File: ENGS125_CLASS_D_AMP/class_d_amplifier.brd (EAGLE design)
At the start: 89.8 x 64.8 mm, 24 parts, among them J1 BANANA_JACK_CT3151, J2 BANANA_JACK_CT3151, J3 BANANA_JACK_CT3151, J4 BANANA_JACK_CT3151, J5 BANANA_JACK_CT3151, J6 BANANA_JACK_CT3151, M1 BSC050NE2LSATMA1, M2 BSC050NE2LSATMA1, U1 LTC6992TSOT-23, U2 LTC4449

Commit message: Added Thayer shield to silkscreen on layout
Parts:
- added U$1: THAYER, Engs125_lib_UPDATEFeb22_with_logo:THAYER
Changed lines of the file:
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@@
 <layer number="25" name="tNames" color="7" fill="1" visible="yes" active="yes"/>
 <layer number="26" name="bNames" color="7" fill="1" visible="yes" active="yes"/>
-<layer number="27" name="tValues" color="7" fill="1" visible="no" active="yes"/>
+<layer number="27" name="tValues" color="7" fill="1" visible="yes" active="yes"/>
 <layer number="28" name="bValues" color="7" fill="1" visible="no" active="yes"/>
 <layer number="29" name="tStop" color="7" fill="3" visible="no" active="yes"/>
@@
 <layer number="44" name="Drills" color="7" fill="1" visible="no" active="yes"/>
 <layer number="45" name="Holes" color="7" fill="1" visible="yes" active="yes"/>
-<layer number="46" name="Milling" color="3" fill="1" visible="no" active="yes"/>
-<layer number="47" name="Measures" color="7" fill="1" visible="no" active="yes"/>
-<layer number="48" name="Document" color="7" fill="1" visible="no" active="yes"/>
-<layer number="49" name="Reference" color="7" fill="1" visible="no" active="yes"/>
+<layer number="46" name="Milling" color="3" fill="1" visible="yes" active="yes"/>
+<layer number="47" name="Measures" color="7" fill="1" visible="yes" active="yes"/>
+<layer number="48" name="Document" color="7" fill="1" visible="yes" active="yes"/>
+<layer number="49" name="Reference" color="7" fill="1" visible="yes" active="yes"/>
 <layer number="51" name="tDocu" color="7" fill="1" visible="yes" active="yes"/>
 <layer number="52" name="bDocu" color="7" fill="1" visible="yes" active="yes"/>
@@
 <attribute name="NAME" x="62.738" y="32.766" size="1.016" layer="25" font="fixed" rot="R270"/>
 </element>
+<element name="U$1" library="Engs125_lib_UPDATEFeb22_with_logo" package="THAYER" value="THAYER" x="72.517" y="50.419" smashed="yes"/>
 </elements>
 <signals>

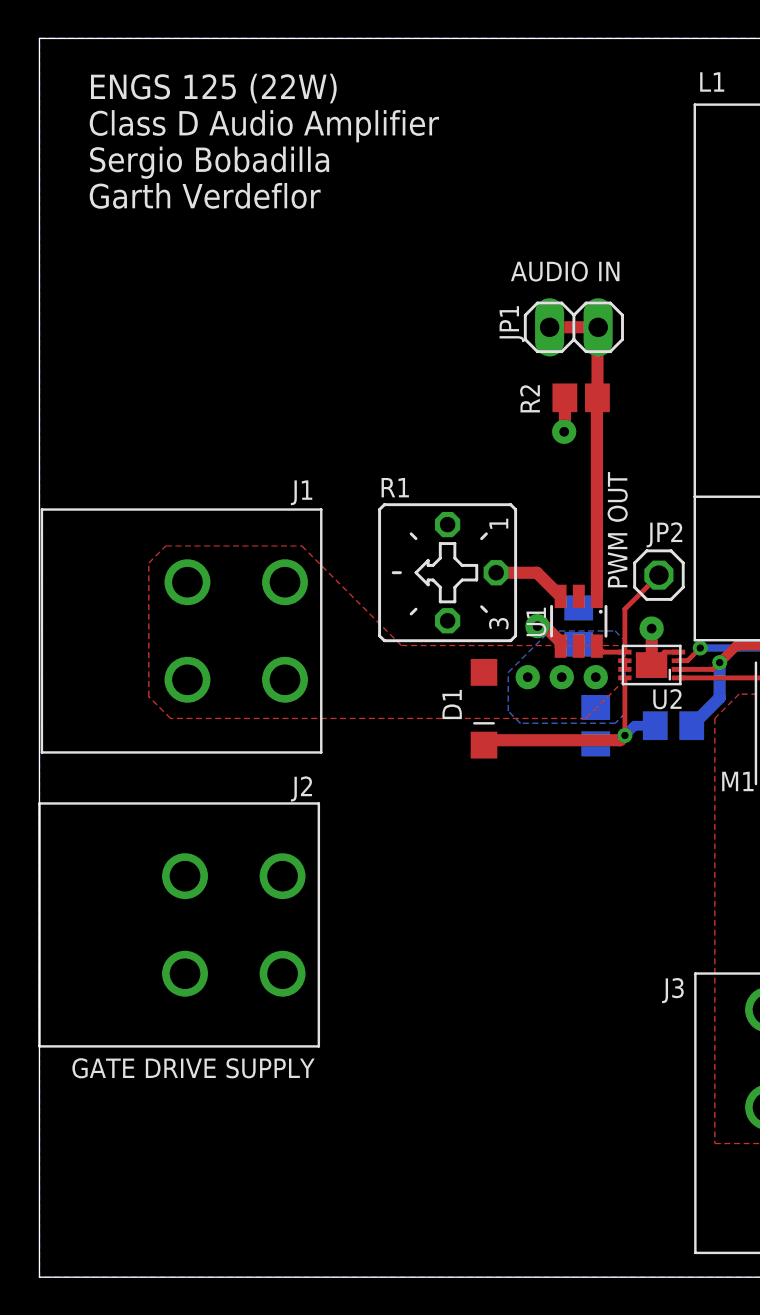
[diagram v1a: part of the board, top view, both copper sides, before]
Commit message: Reformatted silkscreen info with logo
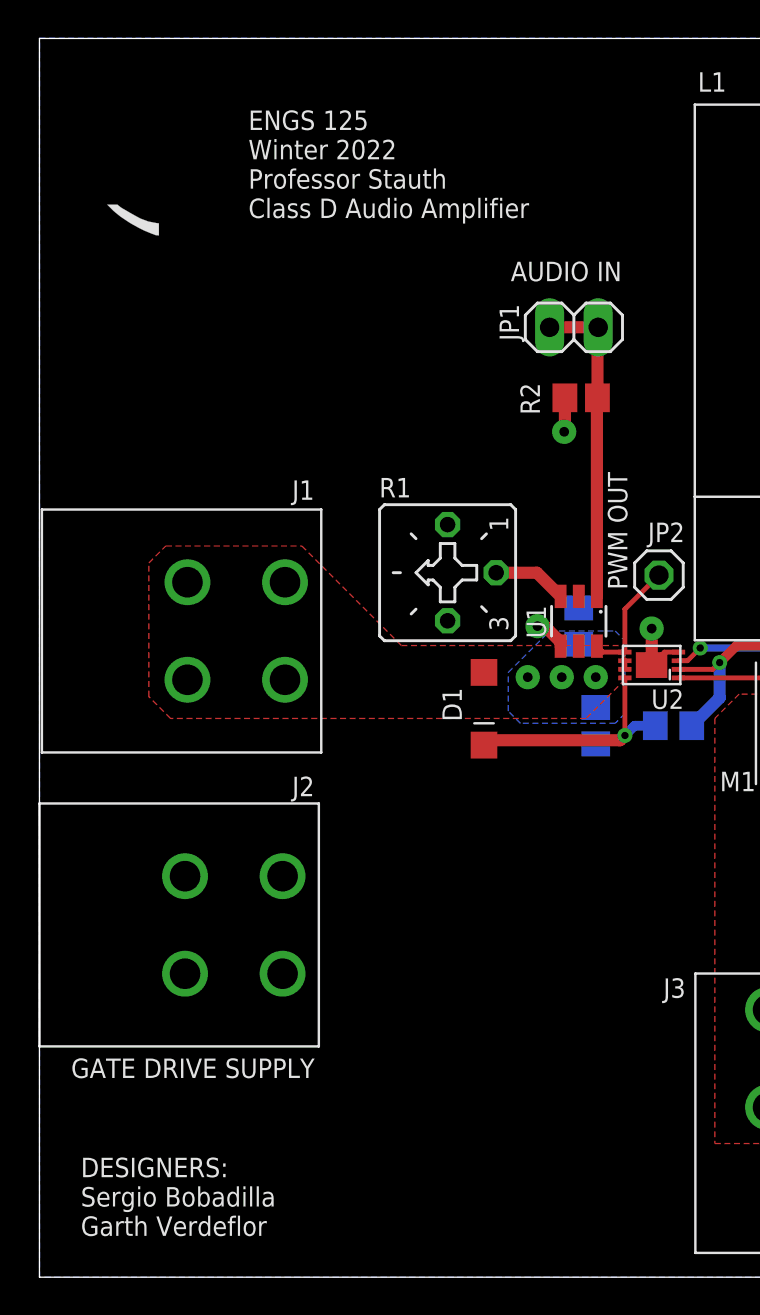
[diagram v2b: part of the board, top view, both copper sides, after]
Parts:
- moved U$1 69.8 mm to (2.79, 54.5)
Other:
- board text added: "DESIGNERS: Sergio Bobadilla Garth Verdeflor"
- board text added: "ENGS 125 Winter 2022 Professor Stauth Class D Audio Amplifier"
- board text removed: "ENGS 125 (22W) Class D Audio Amplifier Sergio Bobadilla Garth Verdeflor"
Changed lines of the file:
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@@
 <layer number="2" name="Route2" color="1" fill="3" visible="yes" active="yes"/>
 <layer number="3" name="Route3" color="4" fill="3" visible="yes" active="yes"/>
-<layer number="4" name="Route4" color="18" fill="1" visible="no" active="yes"/>
-<layer number="5" name="Route5" color="19" fill="1" visible="no" active="yes"/>
+<layer number="4" name="Route4" color="18" fill="1" visible="yes" active="yes"/>
+<layer number="5" name="Route5" color="19" fill="1" visible="yes" active="yes"/>
 <layer number="6" name="Route6" color="25" fill="1" visible="no" active="yes"/>
 <layer number="7" name="Route7" color="26" fill="1" visible="no" active="yes"/>
@@
 <wire x1="89.84" y1="64.76" x2="0" y2="64.76" width="0" layer="20"/>
 <wire x1="0" y1="64.76" x2="0" y2="0" width="0" layer="20"/>
-<text x="2.54" y="55.88" size="1.27" layer="21" font="fixed">ENGS 125 (22W)
+<text x="10.922" y="55.372" size="1.016" layer="21" font="fixed" distance="51">ENGS 125
+Winter 2022
+Professor Stauth
 Class D Audio Amplifier
-Sergio Bobadilla
-Garth Verdeflor</text>
+</text>
 <text x="24.638" y="52.07" size="1.016" layer="21" font="fixed">AUDIO IN</text>
 <text x="1.651" y="10.414" size="1.016" layer="21" font="fixed">GATE DRIVE SUPPLY</text>
@@
 <vertex x="71.117678125" y="57.15"/>
 </polygon>
+<text x="2.159" y="2.159" size="1.016" layer="21" font="fixed" distance="51">DESIGNERS:
+Sergio Bobadilla
+Garth Verdeflor</text>
 </plain>
 <attributes>
@@
 <attribute name="NAME" x="62.738" y="32.766" size="1.016" layer="25" font="fixed" rot="R270"/>
 </element>
-<element name="U$1" library="Engs125_lib_UPDATEFeb22_with_logo" package="THAYER" value="THAYER" x="72.517" y="50.419" smashed="yes"/>
+<element name="U$1" library="Engs125_lib_UPDATEFeb22_with_logo" package="THAYER" value="THAYER" x="2.794" y="54.483" smashed="yes"/>
 </elements>
 <signals>

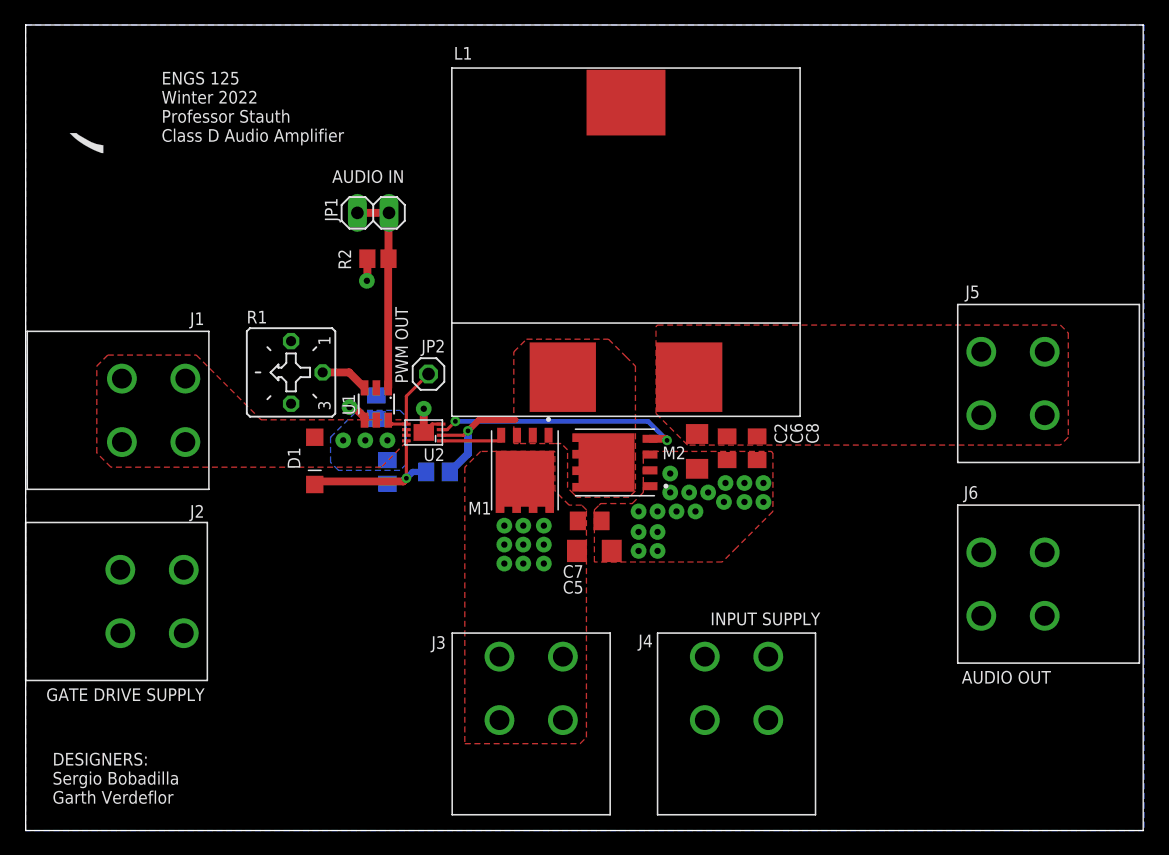
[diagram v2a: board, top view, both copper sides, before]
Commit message: Implemented edits from discussion with Stauth: GND pins, Gate pins, and extra input cap.
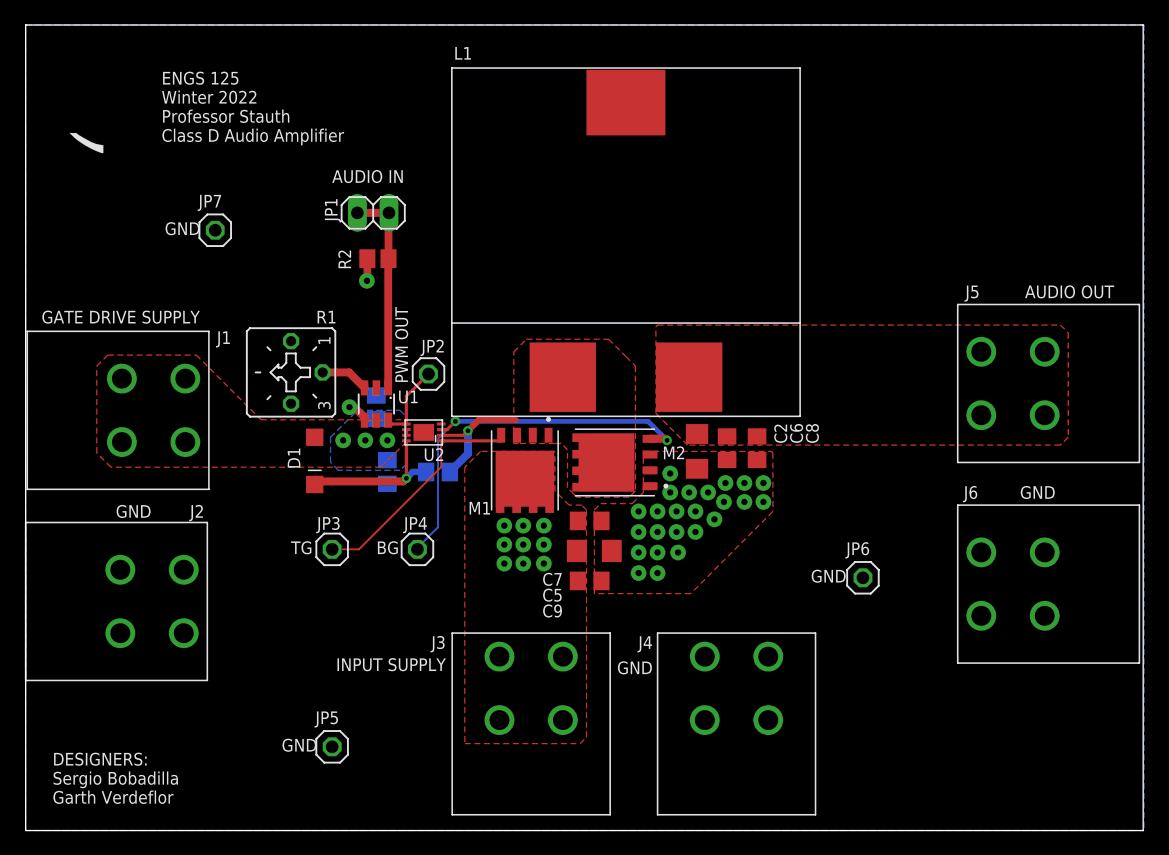
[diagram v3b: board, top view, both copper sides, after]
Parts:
- added C9: 1uF, Engs125_library:C0805
- added JP3, JP4, JP5, JP6, JP7: (no value), Engs125_lib_UPDATEFeb22:1X01
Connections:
- net BG: now also JP4.1
- net GND: now also C9.2, JP5.1, JP6.1, JP7.1
- net TG: now also JP3.1
- net VIN: now also C9.1
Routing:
- net TG: track 5.27 -> 18.9 mm
- net BG: track 20.5 -> 32.0 mm
- net GND: track 7.15 -> 3.56 mm, vias 21 -> 26
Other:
- board text added: "BG"
- board text added: "GND"
- board text added: "TG"

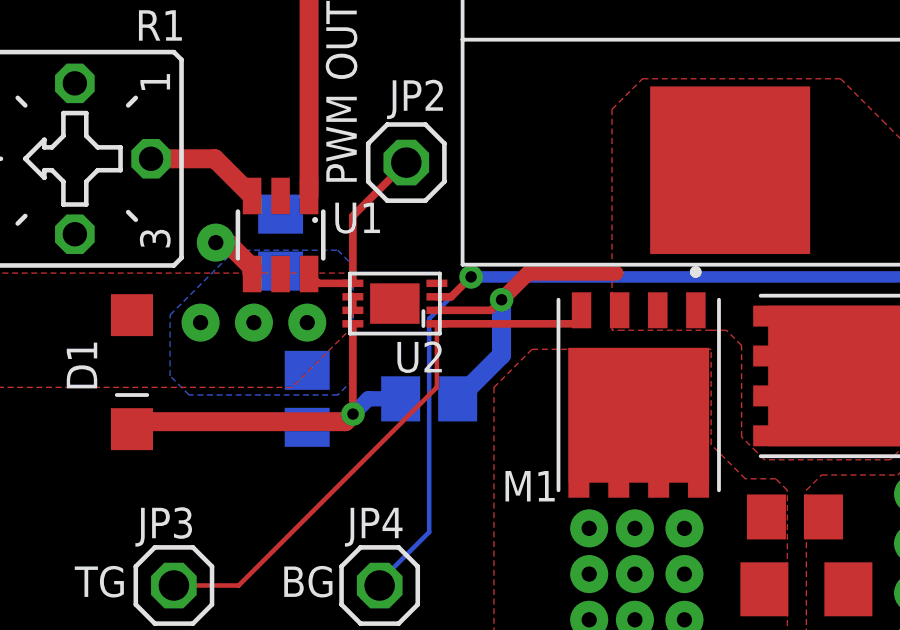
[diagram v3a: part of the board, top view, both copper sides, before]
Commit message: Replaced gate driver IC with LTC4442
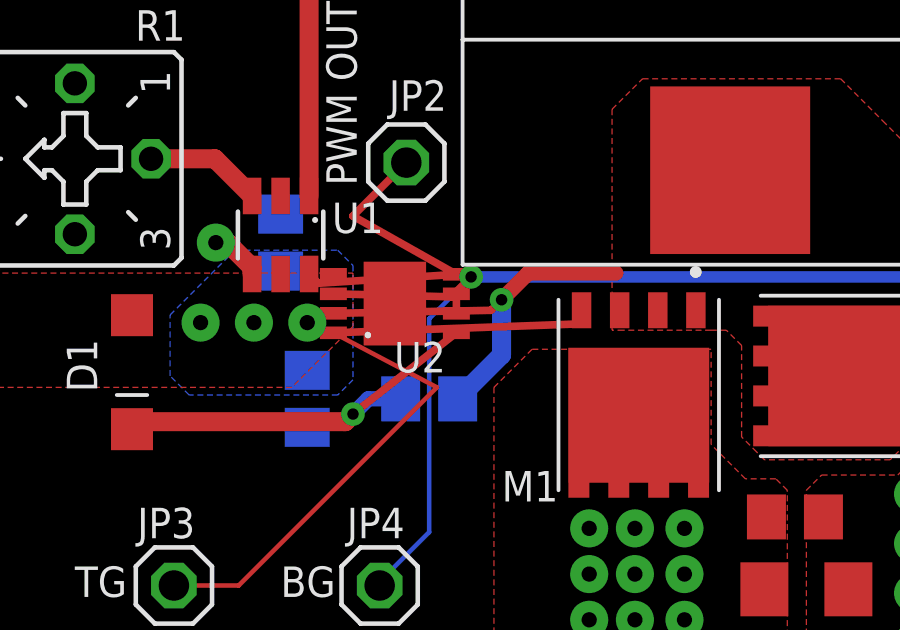
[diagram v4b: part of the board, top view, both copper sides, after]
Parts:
- U2: value LTC4449 -> LTC4442; device Engs125_library:DCB8 -> Engs125_lib_NEW_UPDATE_USE_THIS:LTC4442
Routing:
- net TG: track 18.9 -> 24.1 mm
- net VPWM: track 6.35 -> 11.5 mm
- net BG: track 32.0 -> 35.5 mm
- net VSW: track 10.4 -> 13.8 mm
- net N$2: track 12.4 -> 13.8 mm
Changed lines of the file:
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@@
 <attribute name="NAME" x="34.417" y="61.976" size="1.016" layer="25" font="fixed"/>
 </element>
-<element name="U2" library="Engs125_library" package="DCB8" value="LTC4449" x="32.004" y="32.004" smashed="yes" rot="R90">
+<element name="U2" library="Engs125_lib_NEW_UPDATE_USE_THIS" package="LTC4442" value="LTC4442" x="32.004" y="32.004" smashed="yes" rot="R90">
 <attribute name="NAME" x="33.695" y="30.726" size="1.016" layer="25" font="fixed" rot="R180"/>
 </element>
@@
 <via x="52.451" y="22.352" extent="1-16" drill="0.508" diameter="1.27"/>
 <via x="55.372" y="25.019" extent="1-16" drill="0.508" diameter="1.27"/>
-<wire x1="32.004" y1="32.004" x2="33.404" y2="32.679" width="0" layer="19" extent="1-1"/>
-<wire x1="28.194" y1="34.986" x2="32.004" y2="32.004" width="0" layer="19" extent="1-16"/>
+<wire x1="29.954" y1="32.979" x2="32.004" y2="32.004" width="0" layer="19" extent="1-1"/>
+<wire x1="28.194" y1="34.986" x2="29.954" y2="32.979" width="0" layer="19" extent="1-16"/>
 </signal>
 <signal name="VGG">
@@
 <via x="29.083" y="31.369" extent="1-16" drill="0.508" diameter="1.27"/>
 <via x="27.305" y="31.369" extent="1-16" drill="0.508" diameter="1.27"/>
-<wire x1="30.604" y1="32.229" x2="30.604" y2="31.779" width="0.254" layer="1"/>
+<wire x1="34.054" y1="32.329" x2="34.054" y2="31.679" width="0.254" layer="1"/>
 <polygon width="0.127" layer="1" isolate="0.3048" thermals="no">
 <vertex x="5.715" y="30.353"/>
@@
 <vertex x="25.146" y="28.956"/>
 </polygon>
+<wire x1="29.083" y1="31.369" x2="34.054" y2="31.679" width="0" layer="19" extent="1-1"/>
 </signal>
 <signal name="VPWM">
@@
 <contactref element="JP2" pad="1"/>
 <wire x1="32.385" y1="36.703" x2="30.604" y2="34.922" width="0.254" layer="1"/>
-<wire x1="30.604" y1="34.922" x2="30.604" y2="32.679" width="0.254" layer="1"/>
-<wire x1="30.604" y1="32.679" x2="29.455" y2="32.679" width="0.254" layer="1"/>
+<wire x1="30.604" y1="34.922" x2="34.054" y2="32.979" width="0.254" layer="1"/>
+<wire x1="34.054" y1="32.979" x2="29.455" y2="32.679" width="0.254" layer="1"/>
 <wire x1="29.455" y1="32.679" x2="29.144" y2="32.99" width="0.254" layer="1"/>
 </signal>
@@
 <via x="30.607" y="28.321" extent="1-16" drill="0.381" diameter="0.762"/>
 <wire x1="30.607" y1="28.321" x2="30.604" y2="28.324" width="0.254" layer="1"/>
-<wire x1="30.604" y1="28.324" x2="30.604" y2="31.329" width="0.254" layer="1"/>
+<wire x1="30.604" y1="28.324" x2="34.054" y2="31.029" width="0.254" layer="1"/>
 <wire x1="32.197" y1="28.829" x2="31.115" y2="28.829" width="0.508" layer="16"/>
 <wire x1="30.607" y1="28.321" x2="31.115" y2="28.829" width="0.508" layer="16"/>
@@
 </polygon>
 <via x="35.56" y="32.131" extent="1-16" drill="0.381" diameter="0.762"/>
-<wire x1="33.404" y1="31.779" x2="35.208" y2="31.779" width="0.254" layer="1"/>
+<wire x1="29.954" y1="31.679" x2="35.208" y2="31.779" width="0.254" layer="1"/>
 <wire x1="35.208" y1="31.779" x2="35.56" y2="32.131" width="0.254" layer="1"/>
 <wire x1="34.097" y1="28.829" x2="35.56" y2="30.292" width="0.635" layer="16"/>
@@
 <via x="34.544" y="32.893" extent="1-16" drill="0.381" diameter="0.762"/>
 <wire x1="34.544" y1="32.893" x2="33.88" y2="32.229" width="0.254" layer="1"/>
-<wire x1="33.88" y1="32.229" x2="33.404" y2="32.229" width="0.254" layer="1"/>
+<wire x1="33.88" y1="32.229" x2="29.954" y2="32.329" width="0.254" layer="1"/>
 <contactref element="JP4" pad="1"/>
 <wire x1="34.544" y1="32.893" x2="33.147" y2="31.496" width="0.1524" layer="16"/>
@@
 <contactref element="M1" pad="4"/>
 <wire x1="38.227" y1="31.781" x2="38.227" y2="31.329" width="0.254" layer="1"/>
-<wire x1="38.227" y1="31.329" x2="33.404" y2="31.329" width="0.254" layer="1"/>
+<wire x1="38.227" y1="31.329" x2="29.954" y2="31.029" width="0.254" layer="1"/>
 <contactref element="JP3" pad="1"/>
 <wire x1="24.638" y1="22.606" x2="26.797" y2="22.606" width="0.1524" layer="1"/>
-<wire x1="33.404" y1="29.213" x2="33.404" y2="31.329" width="0.1524" layer="1"/>
+<wire x1="33.404" y1="29.213" x2="29.954" y2="31.029" width="0.1524" layer="1"/>
 <wire x1="26.797" y1="22.606" x2="33.404" y2="29.213" width="0.1524" layer="1"/>
 </signal>
